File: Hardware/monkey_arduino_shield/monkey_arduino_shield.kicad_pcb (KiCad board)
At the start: 2 copper layers, 68.6 x 53.3 mm, 21 parts, among them J1 Speaker_OUT, J3 Screw_Terminal_01x03, J4 Screw_Terminal_01x03, J5 MIC_IN, P1 Power, P2 Analog, P3 Digital, P4 Digital, P5 CONN_01X01, P6 CONN_01X01, P7 CONN_01X01, P8 CONN_01X01, U1 W25Q128JVS, U2 SN74LVC2T45DCUR, U3 SN74LVC2T45DCUR, U4 TPA2005D1DRB

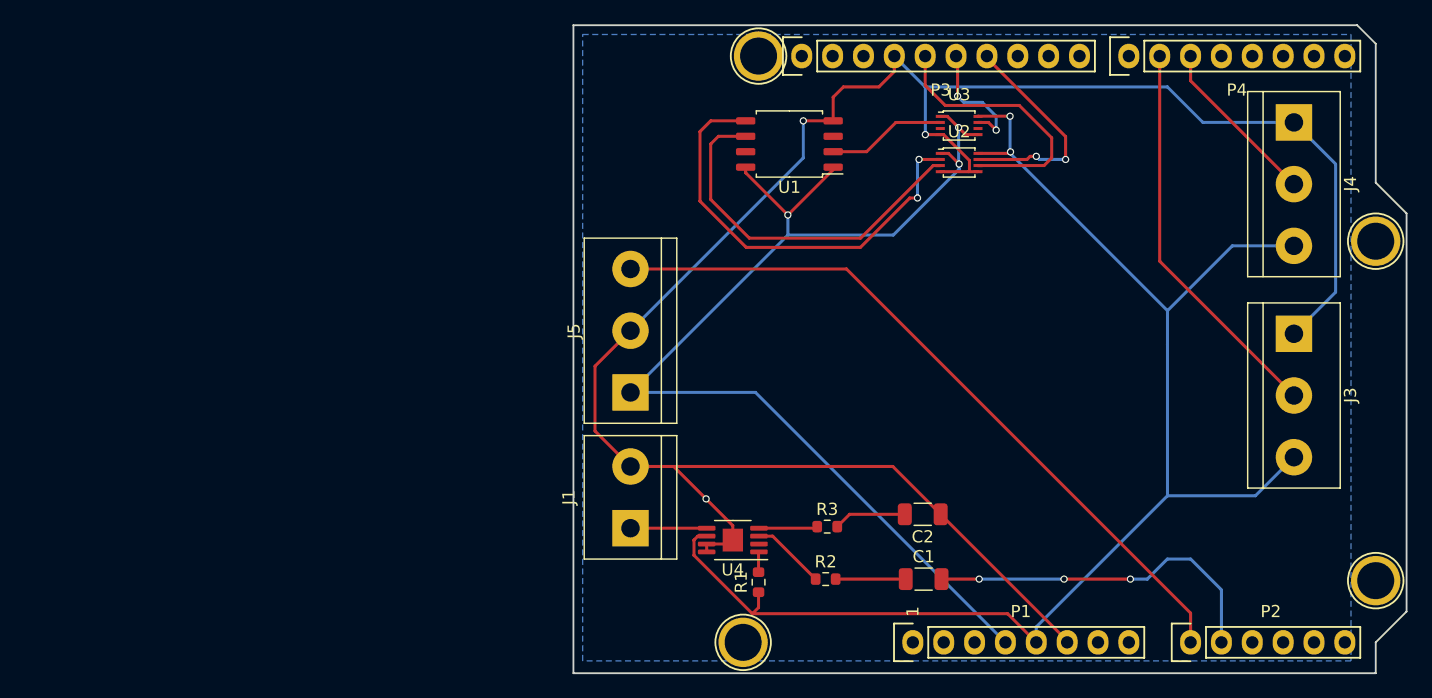
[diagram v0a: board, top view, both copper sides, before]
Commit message: Added power handling to schematic.
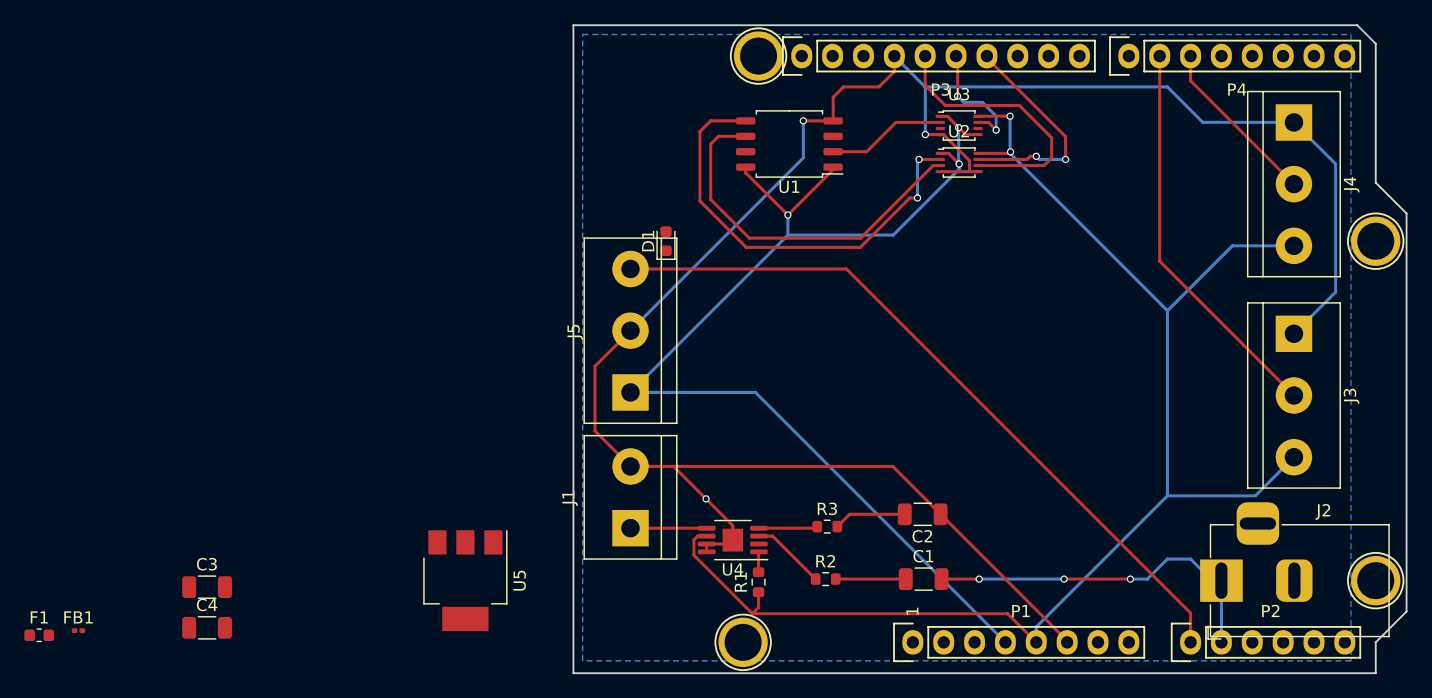
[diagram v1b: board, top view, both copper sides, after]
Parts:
- added C3: 10u, Capacitor_SMD:C_1206_3216Metric, F.Cu at (80.8, 119.3)
- added C4: 10u, Capacitor_SMD:C_1206_3216Metric, F.Cu at (80.8, 122.6)
- added D1: B5819W, Diode_SMD:D_0603_1608Metric, F.Cu at (118.6, 90.8)
- added F1: 500mA, Fuse:Fuse_0603_1608Metric, F.Cu at (67.0, 123.2)
- added FB1: 100 Ohm @ 100 MHz, Inductor_SMD:L_0201_0603Metric, F.Cu at (70.3, 122.9)
- added J2: Barrel_Jack, Connector_BarrelJack:BarrelJack_Horizontal, F.Cu at (164.3, 118.7)
- added U5: AMS1117-5.0, Package_TO_SOT_SMD:SOT-223-3_TabPin2, F.Cu at (102.1, 118.7)
